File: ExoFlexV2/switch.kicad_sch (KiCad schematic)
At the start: 40 parts, among them J23 SWMAX1, J24 SWMIN1, J25 SWMAX2, J26 SWMIN2, J27 SWMAX3, J28 SWMIN3, J29 SWMAX4, J30 SWMAX5, J31 URG1, J32 RESET

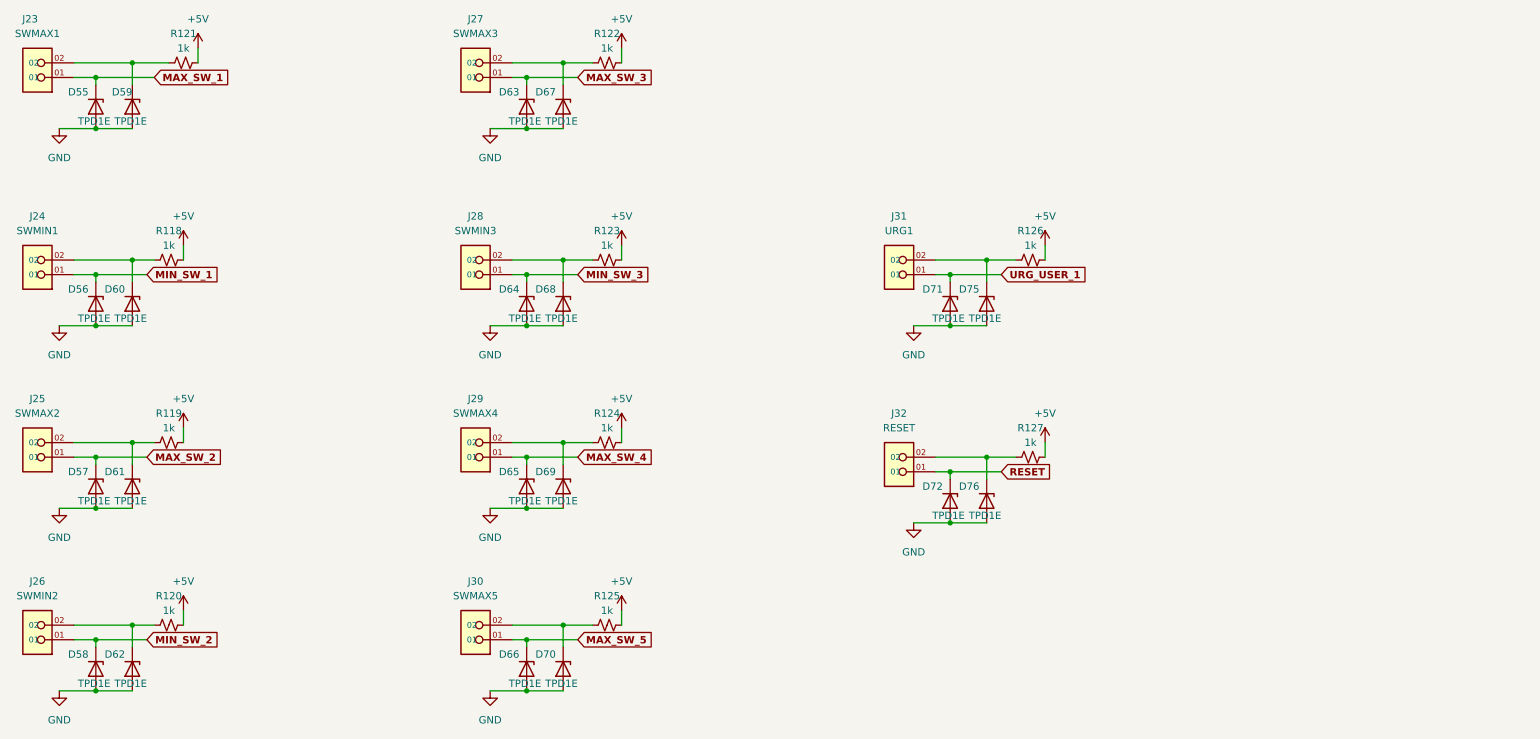
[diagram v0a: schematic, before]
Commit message: Mise à jour signaux STM
- Condo de découplage
- Signaux supplémentaire pour le STM
- Page GND sera pour Multiplexeur
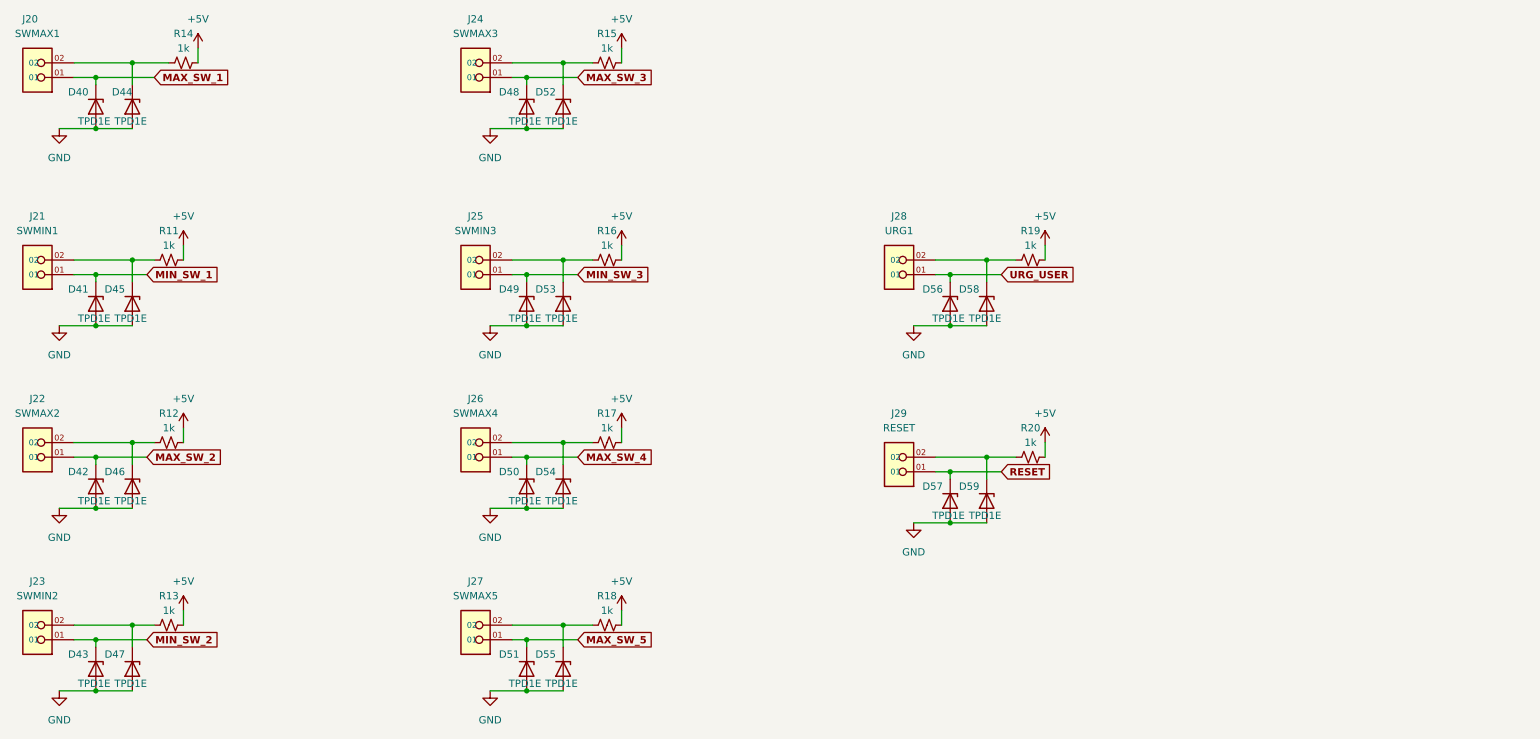
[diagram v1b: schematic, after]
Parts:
- renumbered D55 to D40, D56 to D41, D57 to D42, D58 to D43, D59 to D44, D60 to D45, D61 to D46, D62 to D47, D63 to D48, D64 to D49, D65 to D50, D66 to D51, D67 to D52, D68 to D53, D69 to D54, D70 to D55, D71 to D56, D72 to D57, D75 to D58, D76 to D59, J23 to J20, J24 to J21, J25 to J22, J26 to J23, J27 to J24, J28 to J25, J29 to J26, J30 to J27, J31 to J28, J32 to J29, R118 to R11, R119 to R12, R120 to R13, R121 to R14, R122 to R15, R123 to R16, R124 to R17, R125 to R18, R126 to R19, R127 to R20
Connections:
- net URG_USER_1 renamed URG_USER

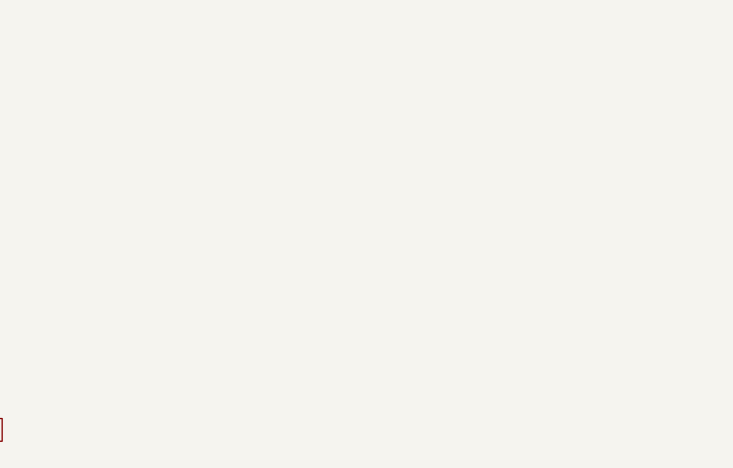
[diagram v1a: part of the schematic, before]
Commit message: Finalisation 1
- Ajout de pages pour la gestion des signaux négatif
- Modification des pages de torque et amplitude
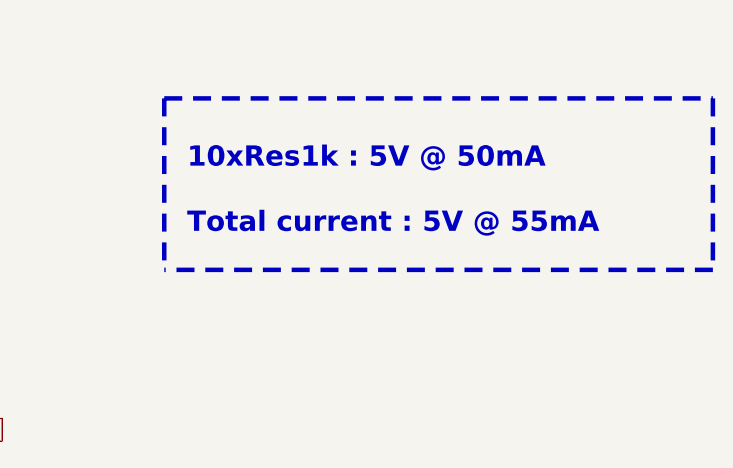
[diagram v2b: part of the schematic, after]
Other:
- note added: "10xRes1k : 5V @ 50mA Total current : 5V @ 55mA"
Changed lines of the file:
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@@
     (stroke (width 0) (type default) (color 0 0 0 0))
+  )
+  (polyline (pts (xy 222.25 33.02) (xy 283.21 33.02))
+    (stroke (width 0.5) (type dash) (color 255 148 44 1))
   )
   (wire (pts (xy 125.73 64.77) (xy 125.73 67.31))
@@
     (stroke (width 0) (type default) (color 0 0 0 0))
   )
+  (polyline (pts (xy 283.21 33.02) (xy 283.21 52.07))
+    (stroke (width 0.5) (type dash) (color 255 148 44 1))
+  )
   (wire (pts (xy 118.11 69.85) (xy 109.22 69.85))
     (stroke (width 0) (type default) (color 0 0 0 0))
@@
     (stroke (width 0) (type default) (color 0 0 0 0))
   )
+  (polyline (pts (xy 222.25 33.02) (xy 222.25 52.07))
+    (stroke (width 0.5) (type dash) (color 255 148 44 1))
+  )
   (wire (pts (xy 49.53 96.52) (xy 49.53 99.06))
     (stroke (width 0) (type default) (color 0 0 0 0))
@@
   (wire (pts (xy 109.22 133.35) (xy 106.68 133.35))
     (stroke (width 0) (type default) (color 0 0 0 0))
+  )
+  (polyline (pts (xy 283.21 52.07) (xy 222.25 52.07))
+    (stroke (width 0.5) (type dash) (color 255 148 44 1))
   )
   (wire (pts (xy 43.18 133.35) (xy 34.29 133.35))
@@
     (stroke (width 0) (type default) (color 0 0 0 0))
   )
+  (text "10xRes1k : 5V @ 50mA\n\nTotal current : 5V @ 55mA" (at 224.79 48.26 0)
+    (effects (font (size 2.25 2.25) (thickness 0.5) bold) (justify left bottom))
+  )
   (global_label "MAX_SW_1" (shape input) (at 44.45 35.56 0) (fields_autoplaced)
